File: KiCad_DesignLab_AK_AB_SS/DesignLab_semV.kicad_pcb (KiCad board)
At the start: 2 copper layers, 57 x 55.8 mm, 31 parts, among them J1 Conn_01x04_Pin, J2 USB_C_Receptacle_USB2.0_16P, SW1 SW_Omron_B3FS, U1 ATmega328PB-A, U2 AMS1117-3.3, U3 CC56-12EWA, U4 DS18B20, U5 BMP280, U6 CH340N, Y1 Crystal

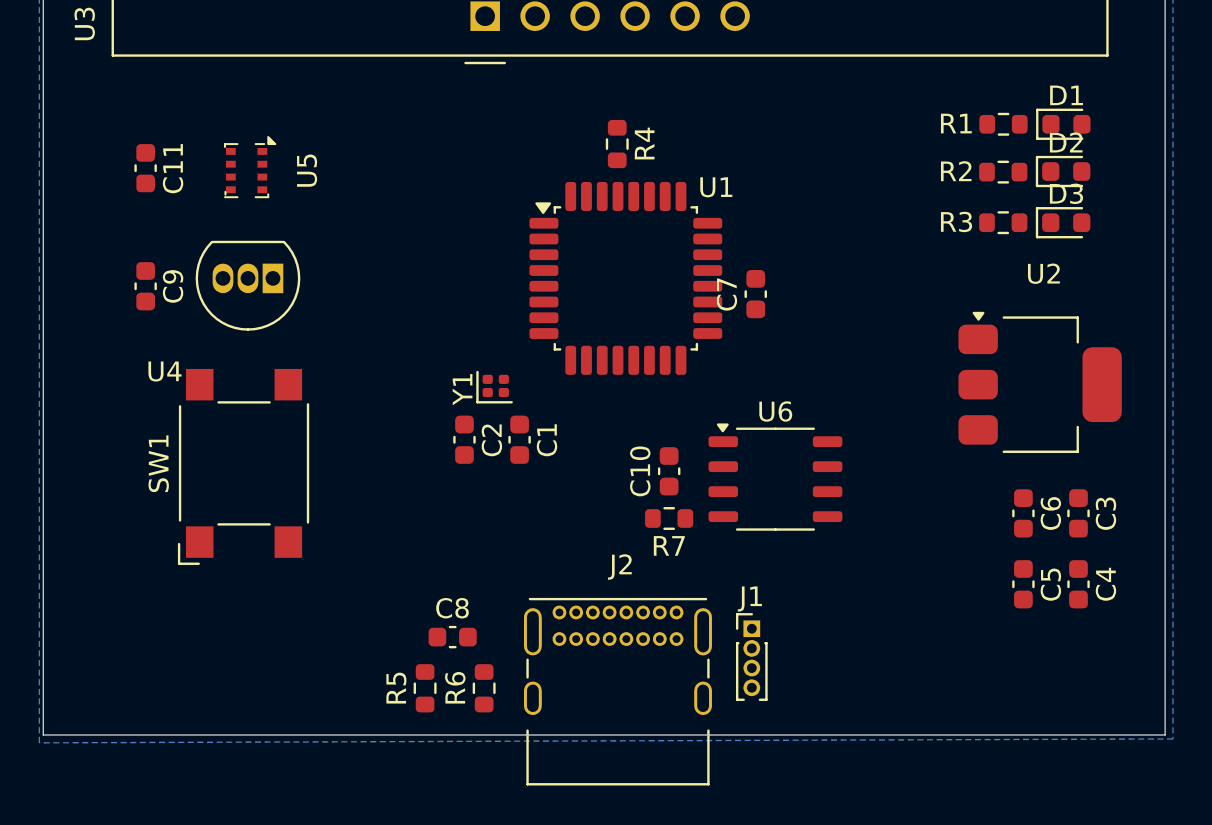
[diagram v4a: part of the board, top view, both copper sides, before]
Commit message: Routed the power lines
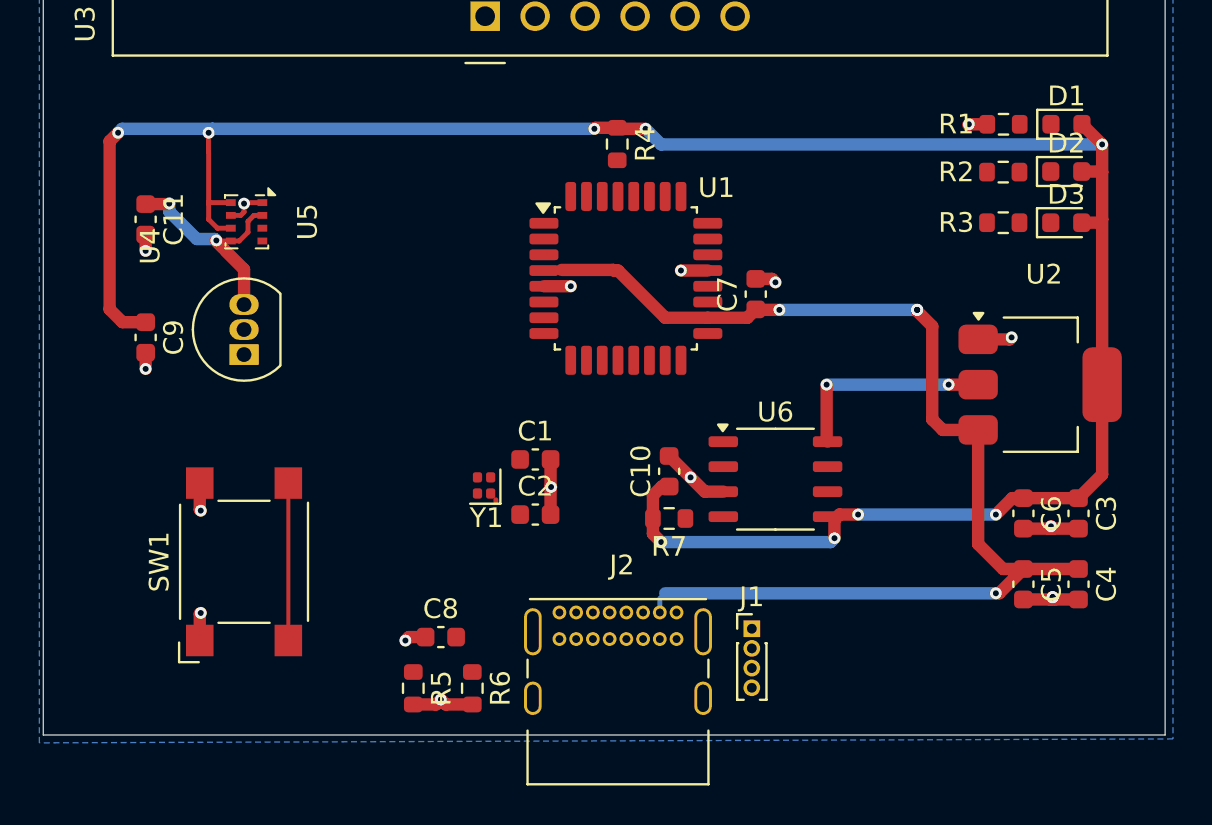
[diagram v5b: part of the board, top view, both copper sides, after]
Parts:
- moved C2 5.23 mm to (132.2, 97.0), turned to 0 degrees
- moved Y1 5.09 mm to (129.6, 95.5), turned to 180 degrees
- moved SW1 5.00 mm to (117.4, 99.4)
- moved U4 4.14 mm to (117.4, 88.9), turned to 90 degrees
- moved C11 2.60 mm to (112.4, 82.0)
- moved C9 2.60 mm to (112.4, 88.0)
- moved U5 2.60 mm to (117.5, 82.1)
- moved C1 1.28 mm to (132.2, 94.2), turned to 0 degrees
- moved C8 0.60 mm to (127.4, 103.2)
- moved R5 0.60 mm to (126.0, 105.8), turned to -90 degrees
- moved R6 0.60 mm to (129.0, 105.8), turned to -90 degrees
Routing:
- net 3.3V: track 0.00 -> 127.8 mm, vias 0 -> 11
- net 5V: track 0.00 -> 71.3 mm, vias 0 -> 6
- net GND: track 0.00 -> 29.6 mm, vias 0 -> 17
- net SW1: track 0.00 -> 8.00 mm

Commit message: Completed PCB v2.0
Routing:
- net SW1: track 8.00 -> 65.0 mm, vias 0 -> 4
- net F: track 0.00 -> 53.6 mm, vias 0 -> 4
- net A: track 0.00 -> 49.1 mm, vias 0 -> 4
- net Net-(U1-PE1): track 0.00 -> 46.6 mm, vias 0 -> 4
- net C: track 0.00 -> 41.5 mm, vias 0 -> 4
- net Net-(U1-PE2): track 0.00 -> 34.9 mm, vias 0 -> 2
- net B: track 0.00 -> 34.9 mm, vias 0 -> 2
- net DPX: track 0.00 -> 32.5 mm, vias 0 -> 4
- net 5V: track 71.3 -> 102.7 mm, vias 6 -> 8
- net E: track 0.00 -> 30.6 mm, vias 0 -> 2
- net Net-(U1-PE0): track 0.00 -> 30.0 mm, vias 0 -> 2
- net Net-(U6-UD-): track 0.00 -> 27.2 mm, vias 0 -> 6
- net 1W: track 0.00 -> 26.9 mm, vias 0 -> 2
- net CS: track 0.00 -> 24.1 mm, vias 0 -> 2
- net UART_TX: track 0.00 -> 23.2 mm, vias 0 -> 2
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
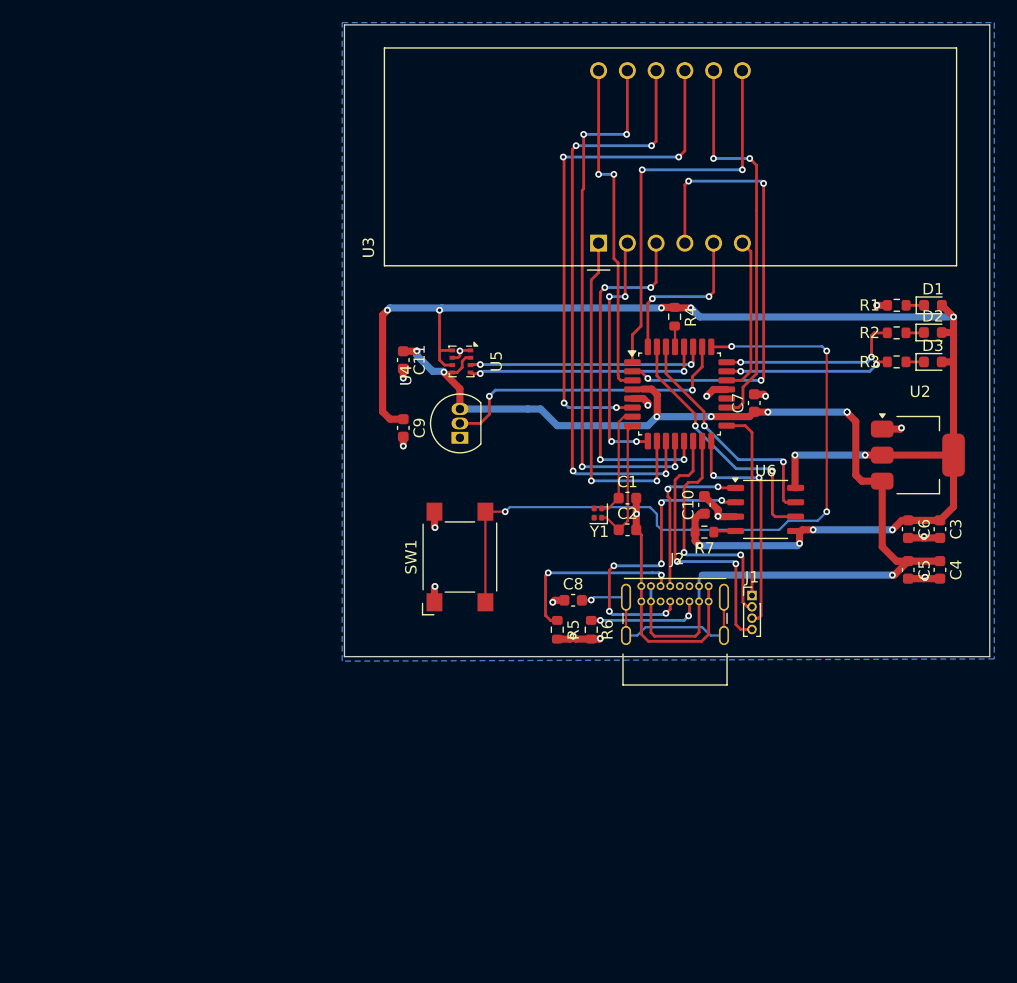
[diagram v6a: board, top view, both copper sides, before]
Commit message: PCB layout modifications
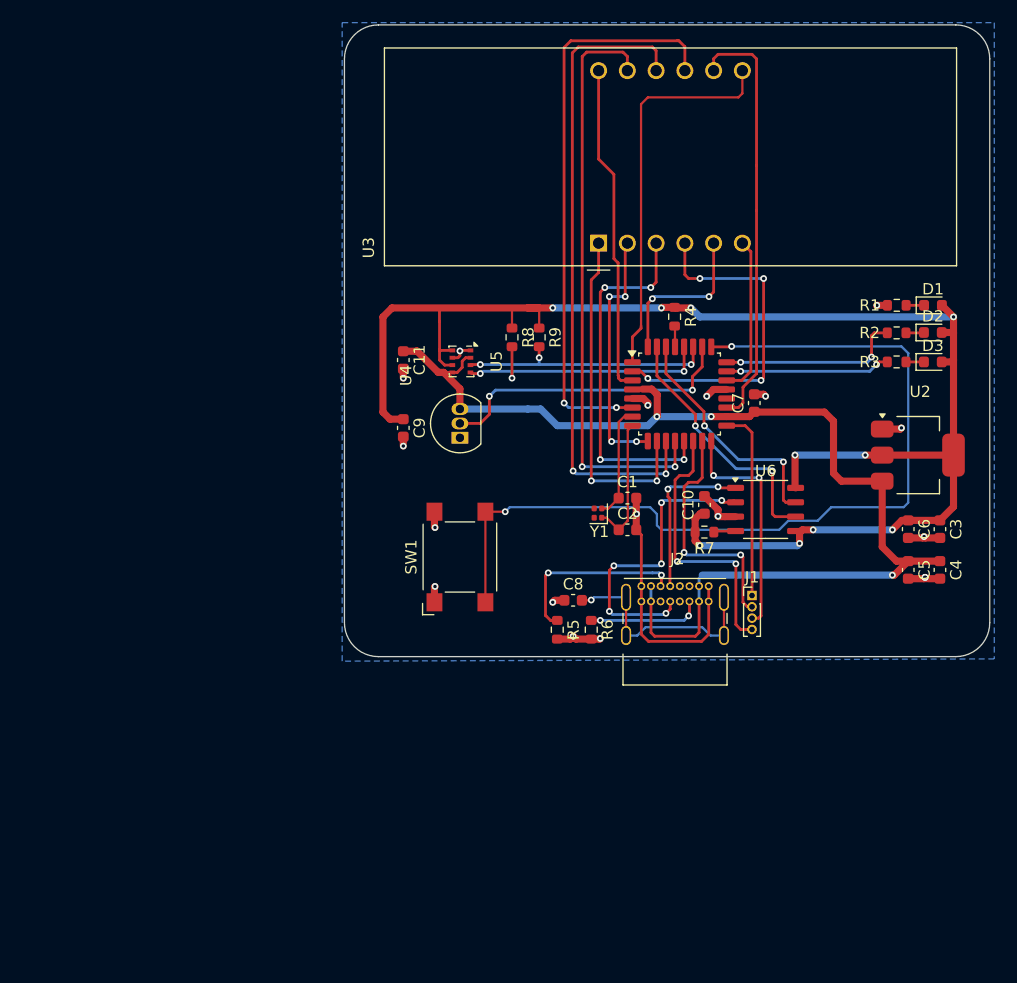
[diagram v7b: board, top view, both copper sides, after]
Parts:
- added R8: 4.7k, Resistor_SMD:R_0603_1608Metric, F.Cu at (122.0, 80.0)
- added R9: 4.7k, Resistor_SMD:R_0603_1608Metric, F.Cu at (124.4, 80.0)
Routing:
- net SW1: track 65.0 -> 78.8 mm, vias 4 -> 2
- net C: track 41.5 -> 30.7 mm
- net Net-(U1-PE1): track 46.6 -> 51.6 mm, vias 4 -> 2
- net 3.3V: track 134.1 -> 138.2 mm, vias 11 -> 10
- net F: track 53.6 -> 57.7 mm, vias 4 -> 2
- net SCL: track 21.0 -> 24.4 mm, vias 2 -> 3
- net A: track 49.1 -> 52.3 mm, vias 4 -> 2
- net Net-(U1-PE2): track 34.9 -> 37.7 mm, vias 2 -> 0
- net SDA: track 21.2 -> 22.7 mm, vias 2 -> 3
- net Net-(U1-PE0): track 30.0 -> 29.2 mm, vias 2 -> 0
- net B: track 34.9 -> 34.5 mm, vias 2 -> 0
- net 5V: track 102.7 -> 102.3 mm, vias 8 -> 3
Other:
- outline, holes or cut-outs redrawn

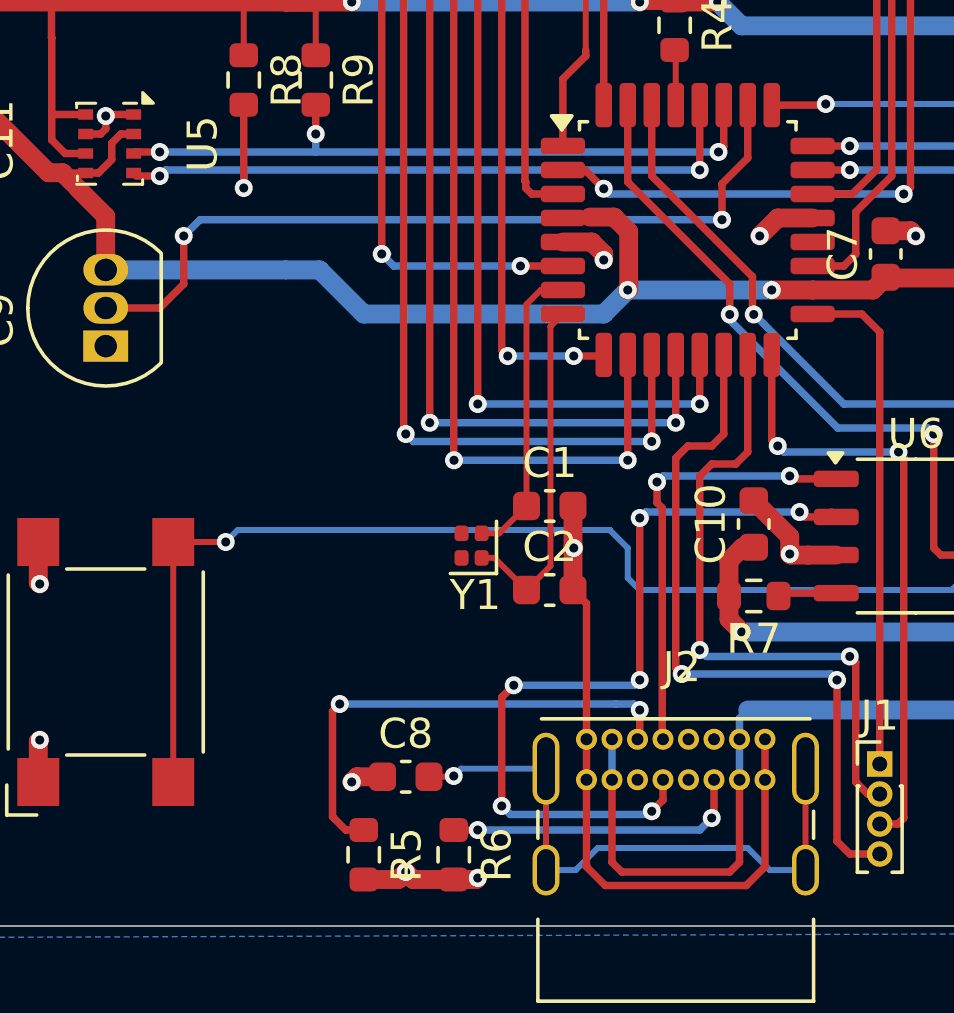
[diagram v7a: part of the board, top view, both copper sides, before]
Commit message: Some DRC fixes
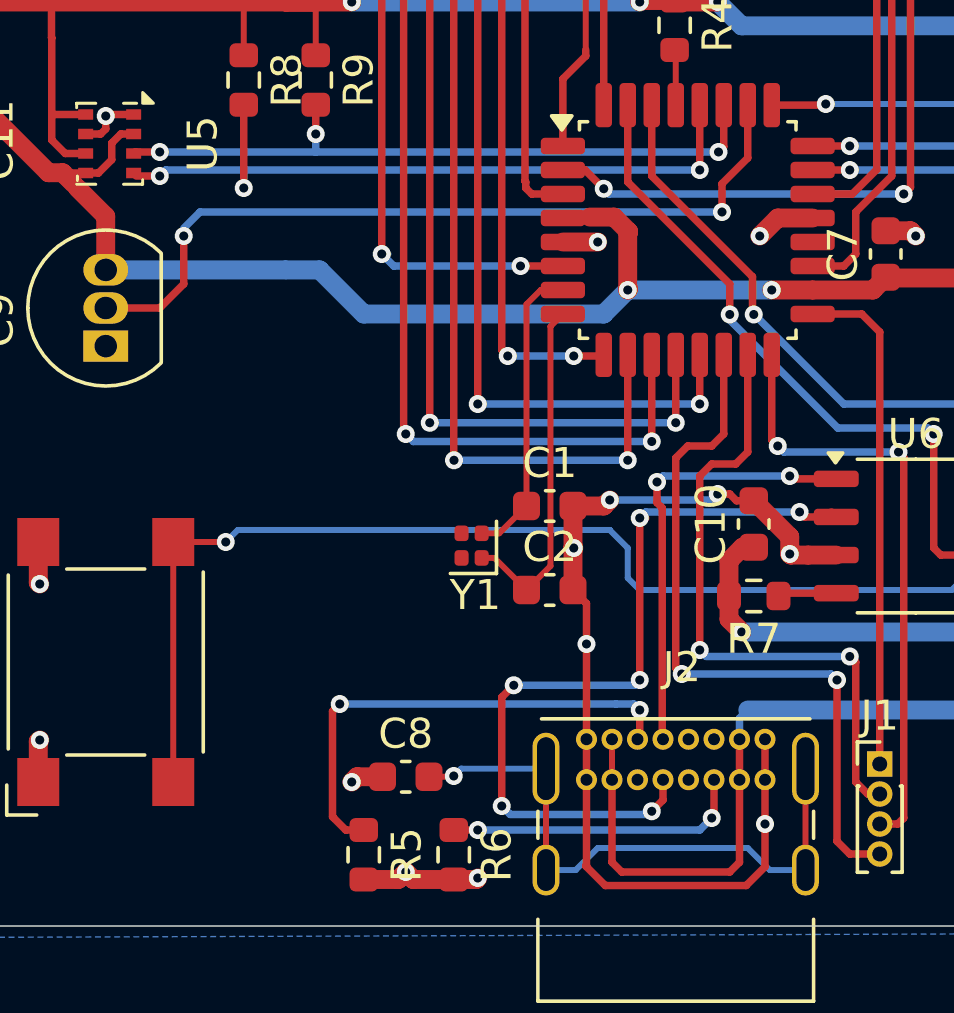
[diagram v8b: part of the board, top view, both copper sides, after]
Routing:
- net GND: track 51.9 -> 57.6 mm, vias 18 -> 22
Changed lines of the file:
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@@
 	)
 	(segment
-		(start 133.425 103.325)
-		(end 133.425 101.975)
-		(width 0.25)
-		(layer "F.Cu")
-		(net 2)
-	)
-	(segment
 		(start 139 94.025)
 		(end 140.2 95.225)
@@
 	)
 	(segment
-		(start 133.425 106.175)
-		(end 133.425 103.325)
-		(width 0.25)
+		(start 134 94.2)
+		(end 134.2 94)
+		(width 0.63)
 		(layer "F.Cu")
 		(net 2)
@@
 	)
 	(segment
+		(start 138.749 106.851)
+		(end 134.051 106.851)
+		(width 0.25)
+		(layer "F.Cu")
+		(net 2)
+	)
+	(segment
+		(start 133.425 106.175)
+		(end 133.425 103.325)
+		(width 0.25)
+		(layer "F.Cu")
+		(net 2)
+	)
+	(segment
 		(start 126.625 103.225)
 		(end 125.775 103.225)
@@
 	)
 	(segment
+		(start 133.425 101.975)
+		(end 133.425 103.325)
+		(width 0.25)
+		(layer "F.Cu")
+		(net 2)
+	)
+	(segment
 		(start 125.775 103.225)
 		(end 125.6 103.4)
@@
 	)
 	(segment
+		(start 132.975 94.2)
+		(end 134 94.2)
+		(width 0.63)
+		(layer "F.Cu")
+		(net 2)
+	)
+	(segment
 		(start 158.515 97.715)
 		(end 158.4 97.6)
@@
 	)
 	(segment
+		(start 132.6375 85.4)
+		(end 133.8 85.4)
+		(width 0.63)
+		(layer "F.Cu")
+		(net 2)
+	)
+	(segment
 		(start 154.2 77.2)
 		(end 154.23 77.17)
@@
 	)
 	(segment
-		(start 133.6 85.4)
-		(end 132.6375 85.4)
-		(width 0.63)
+		(start 133.4 106.2)
+		(end 133.425 106.175)
+		(width 0.25)
 		(layer "F.Cu")
 		(net 2)
@@
 	(segment
 		(start 133.425 101.975)
-		(end 133.425 97.45)
+		(end 133.425 98.8)
 		(width 0.25)
 		(layer "F.Cu")
@@
 	)
 	(segment
+		(start 139.375 103.325)
+		(end 139.375 101.975)
+		(width 0.25)
+		(layer "F.Cu")
+		(net 2)
+	)
+	(segment
 		(start 155.1625 77.17)
 		(end 154.23 77.17)
@@
 	)
 	(segment
-		(start 134.051 106.851)
-		(end 133.4 106.2)
-		(width 0.25)
-		(layer "F.Cu")
-		(net 2)
-	)
-	(segment
 		(start 140.9625 84.6)
 		(end 139.8 84.6)
@@
 	)
 	(segment
+		(start 139 94.025)
+		(end 138.425 94.025)
+		(width 0.25)
+		(layer "F.Cu")
+		(net 2)
+	)
+	(segment
 		(start 118.33 81.15)
 		(end 117.45 81.15)
@@
 	)
 	(segment
-		(start 133.4 106.2)
-		(end 133.425 106.175)
-		(width 0.25)
-		(layer "F.Cu")
-		(net 2)
-	)
-	(segment
 		(start 143.4 85.025)
 		(end 144.225 85.025)
@@
 	)
 	(segment
-		(start 139.375 103.325)
-		(end 139.375 101.975)
+		(start 138.425 94.025)
+		(end 138.2 93.8)
 		(width 0.25)
 		(layer "F.Cu")
@@
 	)
 	(segment
-		(start 138.749 106.851)
-		(end 134.051 106.851)
+		(start 139.375 106.225)
+		(end 138.749 106.851)
+		(width 0.25)
+		(layer "F.Cu")
+		(net 2)
+	)
+	(segment
+		(start 139.375 103.325)
+		(end 139.375 106.225)
 		(width 0.25)
 		(layer "F.Cu")
@@
 	)
 	(segment
-		(start 134 85.8)
-		(end 133.6 85.4)
-		(width 0.63)
+		(start 134.051 106.851)
+		(end 133.4 106.2)
+		(width 0.25)
 		(layer "F.Cu")
 		(net 2)
@@
 	)
 	(segment
-		(start 139.375 106.225)
-		(end 138.749 106.851)
+		(start 132.975 94.2)
+		(end 132.975 95.575)
+		(width 0.63)
+		(layer "F.Cu")
+		(net 2)
+	)
+	(segment
+		(start 133.425 98.8)
+		(end 133.425 97.45)
 		(width 0.25)
 		(layer "F.Cu")
@@
 	)
 	(segment
-		(start 132.975 94.2)
-		(end 132.975 95.575)
-		(width 0.63)
+		(start 138.2 93.8)
+		(end 137.8 93.8)
+		(width 0.25)
 		(layer "F.Cu")
 		(net 2)
@@
 	)
 	(segment
-		(start 134 86)
-		(end 134 85.8)
-		(width 0.63)
-		(layer "F.Cu")
-		(net 2)
-	)
-	(segment
 		(start 140.81 95.835)
 		(end 141.75 95.835)
@@
 	)
 	(segment
-		(start 139.375 103.325)
-		(end 139.375 106.225)
-		(width 0.25)
-		(layer "F.Cu")
-		(net 2)
-	)
-	(segment
 		(start 127.15 106.65)
 		(end 127.4 106.4)
@@
 	)
 	(via
+		(at 134.2 94)
+		(size 0.6)
+		(drill 0.3)
+		(layers "F.Cu" "B.Cu")
+		(net 2)
+	)
+	(via
 		(at 125.6 103.4)
 		(size 0.6)
@@
 	)
 	(via
-		(at 140.2 95.8)
+		(at 133.8 85.4)
 		(size 0.6)
 		(drill 0.3)
@@
 	)
 	(via
-		(at 154.23 77.17)
+		(at 133.425 98.8)
 		(size 0.6)
 		(drill 0.3)
@@
 	)
 	(via
-		(at 156.4 88)
+		(at 140.2 95.8)
+		(size 0.6)
+		(drill 0.3)
+		(layers "F.Cu" "B.Cu")
+		(net 2)
+	)
+	(via
+		(at 154.23 77.17)
 		(size 0.6)
 		(drill 0.3)
@@
 	)
 	(via
-		(at 134 86)
+		(at 156.4 88)
 		(size 0.6)
 		(drill 0.3)
@@
 	)
 	(via
+		(at 139.375 104.8)
+		(size 0.6)
+		(drill 0.3)
+		(layers "F.Cu" "B.Cu")
+		(net 2)
+	)
+	(via
 		(at 117.4 81.2)
 		(size 0.6)
@@
 		(net 2)
 	)
+	(via
+		(at 137.8 93.8)
+		(size 0.6)
+		(drill 0.3)
+		(layers "F.Cu" "B.Cu")
+		(net 2)
+	)
+	(segment
+		(start 137.6 94)
+		(end 134.2 94)
+		(width 0.25)
+		(layer "B.Cu")
+		(net 2)
+	)
+	(segment
+		(start 137.8 93.8)
+		(end 137.6 94)
+		(width 0.25)
+		(layer "B.Cu")
+		(net 2)
+	)
 	(segment
 		(start 130.355 95.93)
@@
 	)
 	(segment
-		(start 137.941942 83.458058)
-		(end 137.941942 84.658058)
+		(start 138.8 80.8375)
+		(end 138.8 82.6)
 		(width 0.25)
 		(layer "F.Cu")
@@
 	)
 	(segment
-		(start 138.8 82.6)
-		(end 137.941942 83.458058)
+		(start 137.941942 83.458058)
+		(end 137.941942 84.4)
 		(width 0.25)
 		(layer "F.Cu")
@@
 	)
 	(segment
-		(start 138.8 80.8375)
-		(end 138.8 82.6)
+		(start 138.8 82.6)
+		(end 137.941942 83.458058)
 		(width 0.25)
 		(layer "F.Cu")
@@
 	)
 	(via
-		(at 137.941942 84.658058)
+		(at 137.941942 84.4)
 		(size 0.6)
 		(drill 0.3)
@@
 	)
 	(segment
-		(start 120 85.2)
-		(end 120.541942 84.658058)
+		(start 120 84.941942)
+		(end 120.541942 84.4)
 		(width 0.25)
 		(layer "B.Cu")
@@
 	)
 	(segment
-		(start 120.541942 84.658058)
-		(end 137.941942 84.658058)
+		(start 120.541942 84.4)
+		(end 137.941942 84.4)
 		(width 0.25)
 		(layer "B.Cu")
@@
 	)
 	(segment
+		(start 134.8 87)
+		(end 134.831 86.969)
+		(width 0.63)
+		(layer "F.Cu")
+		(net 44)
+	)
+	(segment
 		(start 154.7 92.7)
 		(end 151.1 92.7)
@@
 	)
 	(segment
-		(start 134.8 87)
-		(end 134.831 86.969)
-		(width 0.63)
-		(layer "F.Cu")
-		(net 44)
-	)
-	(segment
 		(start 142.975 87)
 		(end 140.9625 87)
@@
 	)
 	(segment
+		(start 134.8 85.086789)
+		(end 134.831 85.055789)
+		(width 0.63)
+		(layer "F.Cu")
+		(net 44)
+	)
+	(segment
 		(start 134.831 85.055789)
 		(end 134.344211 84.569)
@@
 	)
 	(segment
-		(start 134.831 86.969)
-		(end 134.831 85.055789)
+		(start 138.525 103.325)
+		(end 138.525 106.075)
+		(width 0.25)
+		(layer "F.Cu")
+		(net 44)
+	)
+	(segment
+		(start 134.8 87)
+		(end 134.8 85.086789)
 		(width 0.63)
 		(layer "F.Cu")
@@
 	)
 	(segment
-		(start 138.525 103.325)
-		(end 138.525 106.075)
+		(start 134.275 101.975)
+		(end 134.275 103.325)
+		(width 0.2)
+		(layer "F.Cu")
+		(net 44)
+	)
+	(segment
+		(start 138.525 101.975)
+		(end 138.525 103.325)
 		(width 0.25)
 		(layer "F.Cu")
@@
 	)
 	(segment
-		(start 134.275 101.975)
-		(end 134.275 103.325)
-		(width 0.25)
-		(layer "B.Cu")
-		(net 44)
-	)
-	(segment
 		(start 138.525 101.275)
 		(end 138.8 101)
@@
 	)
 	(segment
-		(start 138.525 101.975)
-		(end 138.525 103.325)
-		(width 0.25)
-		(layer "B.Cu")
-		(net 44)
-	)
-	(segment
 		(start 123.4 86.33)
 		(end 117.4 86.33)
@@
 		(layer "B.Cu")
 		(hatch edge 0.5)
-		(connect_pads
+		(connect_pads yes
 			(clearance 0.5)
 		)
